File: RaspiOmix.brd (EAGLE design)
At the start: 85 x 56 mm, 49 parts, among them IC1 MCP3424-E/SL, IC2 DS1307

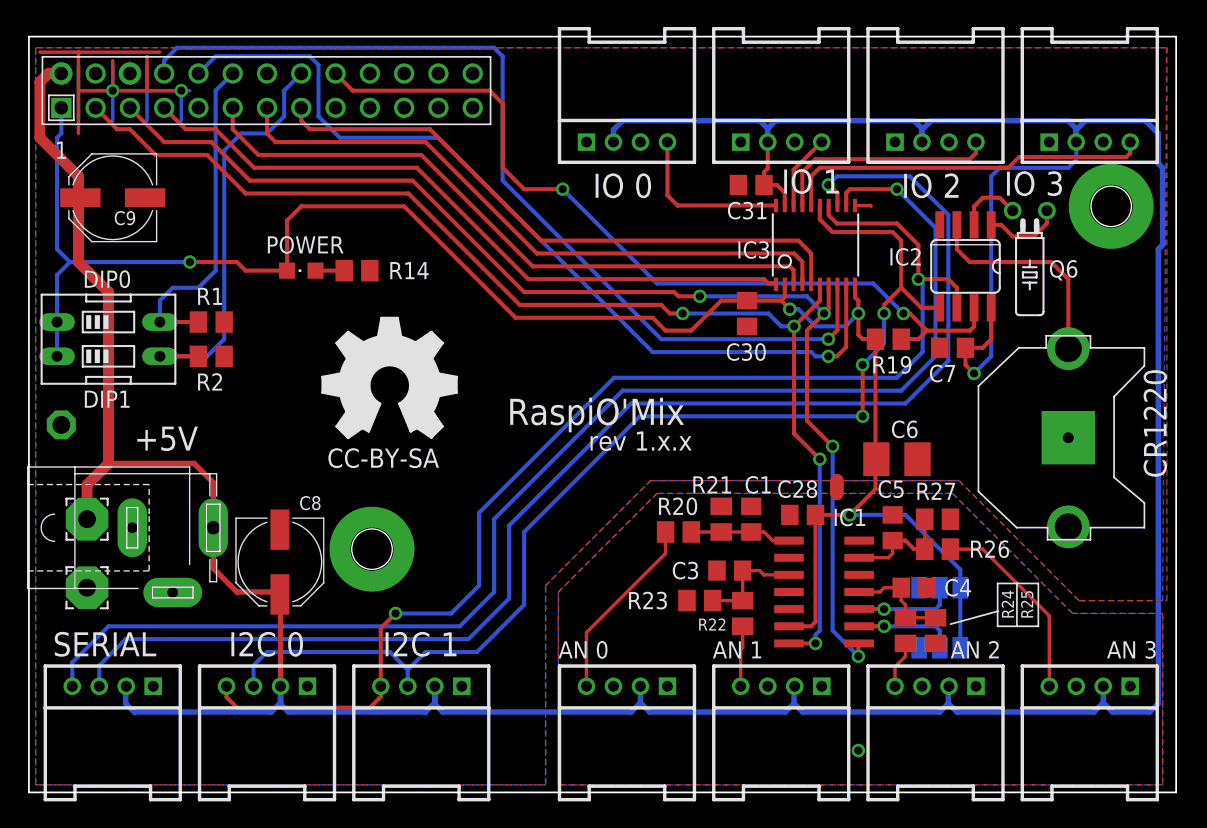
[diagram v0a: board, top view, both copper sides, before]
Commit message: PCB 1.0.8
- Inverse grove connector
- Hole connector linked to VSS
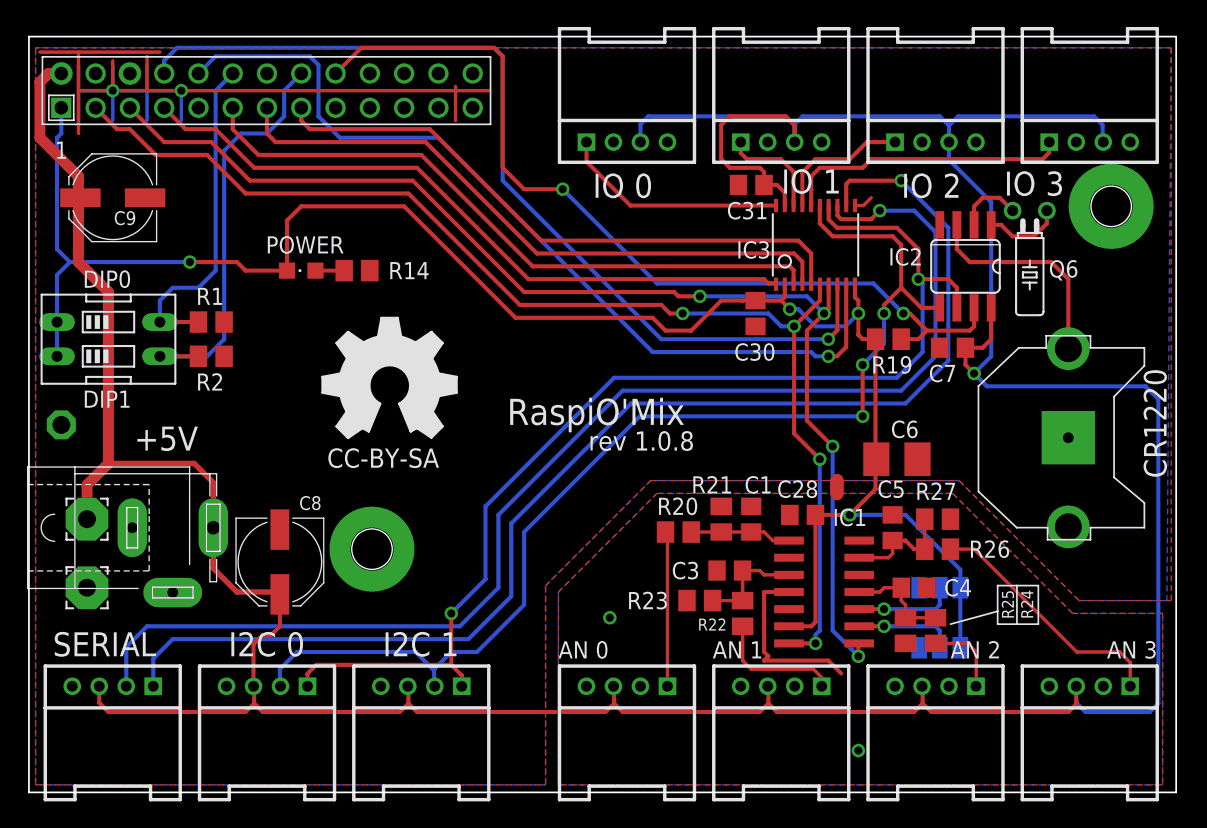
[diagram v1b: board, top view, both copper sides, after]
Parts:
- moved R24 2.22 mm to (67.3, 12.1)
- moved R25 2.22 mm to (65.1, 12.1)
- moved C30 0.63 mm to (54.0, 35.6)
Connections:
- net +5V: now also CON_AN_0.3, CON_AN_1.3, CON_AN_2.3, CON_AN_3.3, CON_I2C_0.3, CON_I2C_1.3, CON_IO_0.3, CON_IO_1.3, CON_IO_2.3, CON_IO_3.3, CON_SERIAL.3; no longer CON_AN_0.2, CON_AN_1.2, CON_AN_2.2, CON_AN_3.2, CON_I2C_0.2, CON_I2C_1.2, CON_IO_0.2, CON_IO_1.2, CON_IO_2.2, CON_IO_3.2, CON_SERIAL.2
- net IO0: now also CON_IO_0.1; no longer CON_IO_0.4
- net IO1: now also CON_IO_1.1; no longer CON_IO_1.4
- net IO2: now also CON_IO_2.1; no longer CON_IO_2.4
- net IO3: now also CON_IO_3.1; no longer CON_IO_3.4
- net N$1: now also CON_AN_0.1; no longer CON_AN_0.4
- net N$2: now also CON_AN_1.1; no longer CON_AN_1.4
- net N$3: now also CON_AN_2.1; no longer CON_AN_2.4
- net N$8: now also CON_AN_3.1; no longer CON_AN_3.4
- net RX: now also CON_SERIAL.1; no longer CON_SERIAL.4
- net SCL: now also CON_I2C_0.1, CON_I2C_1.1; no longer CON_I2C_0.4, CON_I2C_1.4
- net SDA: now also CON_I2C_0.2, CON_I2C_1.2; no longer CON_I2C_0.3, CON_I2C_1.3
- net TX: now also CON_SERIAL.2; no longer CON_SERIAL.3
- net VSS: now also CON_AN_0.4, CON_AN_1.4, CON_AN_2.4, CON_AN_3.4, CON_I2C_0.4, CON_I2C_1.4, CON_IO_0.4, CON_IO_1.4, CON_IO_2.4, CON_IO_3.4, CON_SERIAL.4; no longer CON_AN_0.1, CON_AN_1.1, CON_AN_2.1, CON_AN_3.1, CON_I2C_0.1, CON_I2C_1.1, CON_IO_0.1, CON_IO_1.1, CON_IO_2.1, CON_IO_3.1, CON_SERIAL.1
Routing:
- net VSS: track 52.3 -> 91.3 mm, vias 3 -> 6
- net TX: track 99.9 -> 93.2 mm
- net IO2: track 16.7 -> 10.3 mm
- net SCL: track 90.7 -> 84.6 mm
- net IO3: track 27.3 -> 21.3 mm
- net N$2: track 4.51 -> 9.57 mm
- net IO0: track 12.3 -> 16.8 mm
- net N$8: track 14.6 -> 18.6 mm
- net INTC: track 61.7 -> 65.3 mm
- net RX: track 96.7 -> 93.8 mm
- net +5V: track 283.7 -> 281.2 mm
- net N$1: track 13.9 -> 11.5 mm
- net N$3: track 3.50 -> 5.83 mm
- net IO1: track 5.58 -> 7.80 mm
- net SDA: track 85.2 -> 83.2 mm
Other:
- board text added: "RX"
- board text added: "SCL"
- board text added: "SDA"
- board text added: "TX"
- board text added: "rev 1.0.8"
- board text removed: "rev 1.x.x"
